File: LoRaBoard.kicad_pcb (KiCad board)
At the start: 2 copper layers, 40.8 x 42 mm, 22 parts, among them J1 CONN_01X12, J2 CONN_01X08, J3 CONN_01X09, J4 CONN_COAXIAL, J5 SwitchSPST, J6 CONN_01X01, J7 PWR, U1 im880b, U2 LDO-TPS78233

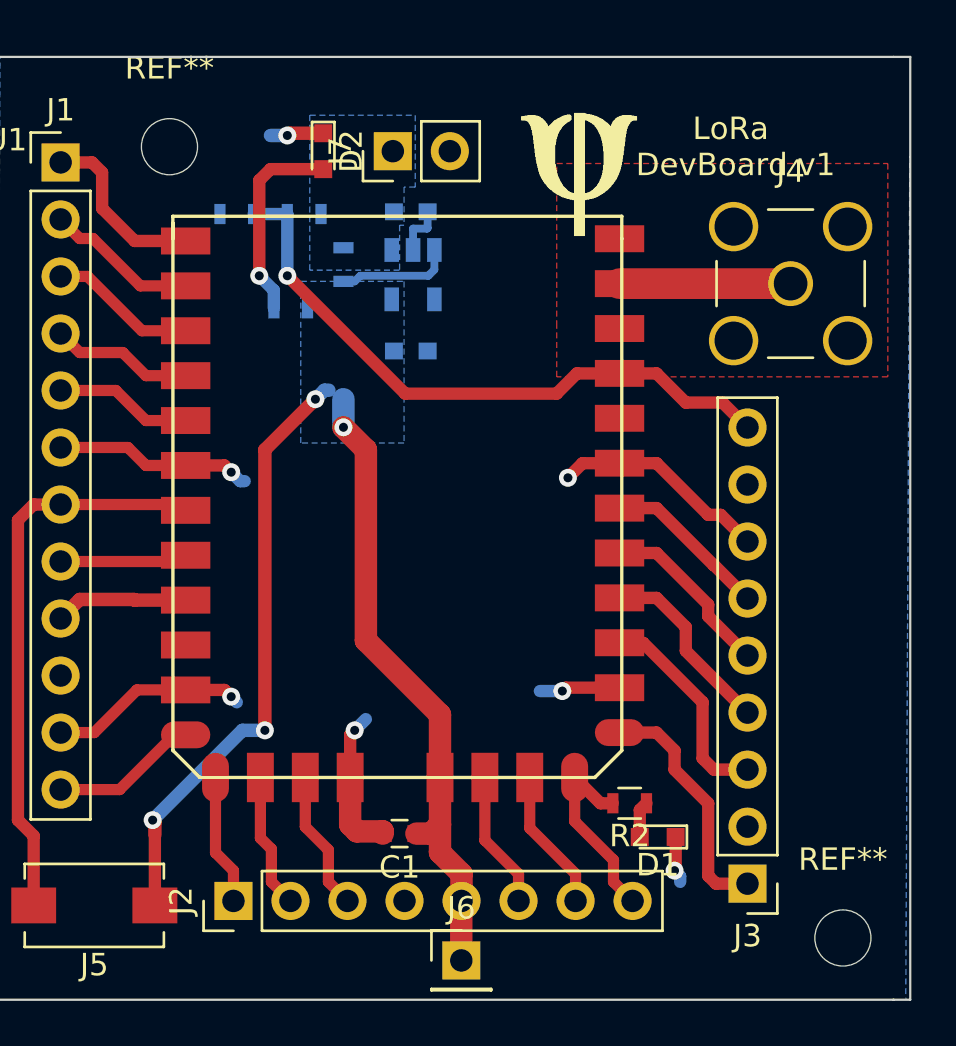
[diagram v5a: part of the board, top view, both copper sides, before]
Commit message: Panelization done, send for Fab
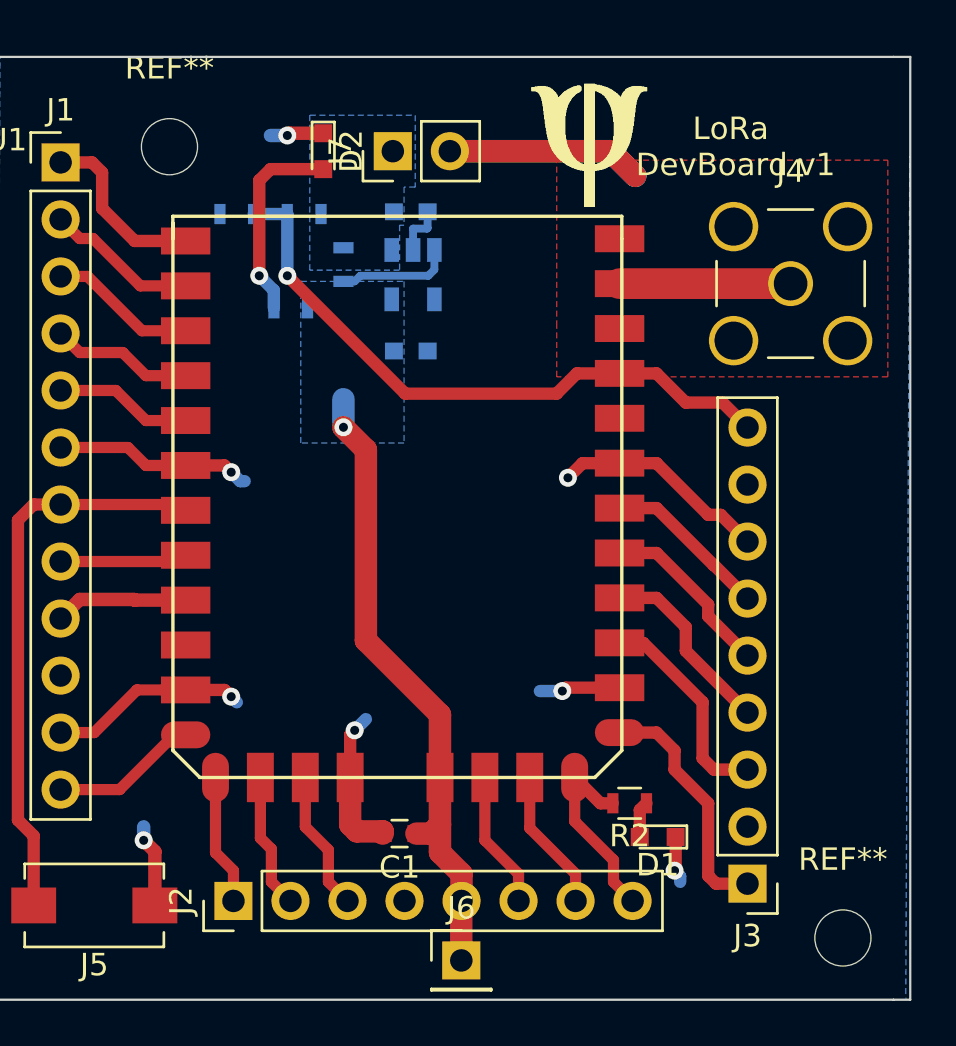
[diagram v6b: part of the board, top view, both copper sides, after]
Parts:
- moved LOGO 1.38 mm to (143.7, 79.2)
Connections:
- J5 pad 1: +3V3 -> GND
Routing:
- net +3V3: track 55.3 -> 28.4 mm, vias 4 -> 1
- net GND: track 44.5 -> 67.6 mm, vias 7 -> 8
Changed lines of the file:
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@@
-(kicad_pcb (version 20170123) (host pcbnew "(2017-04-02 revision 2c33fad45)-master")
+(kicad_pcb (version 4) (host pcbnew 4.0.6-e0-6349~53~ubuntu14.04.1)
   (general
     (links 64)
-    (no_connects 0)
-    (area 117.791667 77.5425 165.953572 121.8425)
+    (no_connects 1)
+    (area 119.949999 77.949999 160.800001 120.050001)
     (thickness 1.6)
     (drawings 12)
-    (tracks 183)
+    (tracks 181)
     (zones 0)
     (modules 22)
@@
   )
   (setup
-    (last_trace_width 1)
+    (last_trace_width 0.6)
     (user_trace_width 0.35)
     (user_trace_width 0.4)
@@
     (trace_clearance 0.2)
     (zone_clearance 0.4)
-    (zone_45_only no)
+    (zone_45_only yes)
     (trace_min 0.2)
     (segment_width 0.2)
@@
       (hpglpenspeed 20)
       (hpglpendiameter 15)
+      (hpglpenoverlay 2)
       (psnegative false)
       (psa4output false)
@@
   )
   (module logo:logo (layer F.Cu)
-    (at 143.25 80.5)
+    (at 143.7 79.2)
     (fp_text reference LOGO (at 0 5) (layer F.SilkS) hide
       (effects (font (thickness 0.3)))
@@
     )
     (pad 1 smd rect (at -2.7 0 180) (size 2 1.6) (layers F.Cu F.Paste F.Mask)
-      (net 2 +3V3))
+      (net 1 GND))
     (pad 2 smd rect (at 2.7 0 180) (size 2 1.6) (layers F.Cu F.Paste F.Mask)
       (net 11 /7))
@@
     )
   )
+  (gr_line (start 160 78) (end 120 78) (layer Edge.Cuts) (width 0.1))
   (gr_line (start 160 78) (end 160.75 78) (layer Edge.Cuts) (width 0.1))
   (gr_line (start 160.75 78) (end 160.75 78) (layer Edge.Cuts) (width 0.1))
@@
   (gr_line (start 120 80) (end 120 80) (layer Edge.Cuts) (width 0.1))
   (gr_line (start 120 78) (end 120 80) (layer Edge.Cuts) (width 0.1))
-  (gr_line (start 160 78) (end 120 78) (layer Edge.Cuts) (width 0.1))
   (gr_text "LoRa\n DevBoard v1\n" (at 152.75 82) (layer F.SilkS)
     (effects (font (size 1 1) (thickness 0.25)))
@@
   (gr_line (start 160 120) (end 120 120) (layer Edge.Cuts) (width 0.1))
   (gr_line (start 120 120) (end 120 80) (layer Edge.Cuts) (width 0.1))
+  (segment (start 126.6 112.9) (end 126.6 112.3) (width 0.6) (layer B.Cu) (net 1))
+  (segment (start 127.1 115.8) (end 127.1 113.4) (width 0.6) (layer F.Cu) (net 1))
+  (segment (start 127.1 113.4) (end 126.6 112.9) (width 0.6) (layer F.Cu) (net 1))
+  (via (at 126.6 112.9) (size 0.8) (drill 0.4) (layers F.Cu B.Cu) (net 1))
+  (segment (start 140.24 82.2) (end 147.4 82.2) (width 1) (layer F.Cu) (net 1))
+  (segment (start 147.4 82.2) (end 148.5 83.3) (width 1) (layer F.Cu) (net 1))
+  (segment (start 140.24 82.2) (end 147.4 82.2) (width 1) (layer B.Cu) (net 1))
+  (segment (start 147.4 82.2) (end 148.5 83.3) (width 1) (layer B.Cu) (net 1))
+  (segment (start 147.4 82.2) (end 148.5 83.3) (width 1) (layer B.Cu) (net 1))
+  (segment (start 140.24 82.2) (end 140.6 82.2) (width 1) (layer B.Cu) (net 1))
   (segment (start 150.5 114.5) (end 150.5 114.75) (width 0.55) (layer B.Cu) (net 1))
   (segment (start 150.25 114.25) (end 150.5 114.5) (width 0.55) (layer B.Cu) (net 1))
@@
   (segment (start 140.75 118.25) (end 140.75 115.61) (width 1) (layer F.Cu) (net 2) (status 30))
   (segment (start 140.75 115.61) (end 140.76 115.6) (width 1) (layer F.Cu) (net 2) (status 30))
-  (segment (start 134.25 93.25) (end 134.649999 92.850001) (width 0.6) (layer B.Cu) (net 2))
-  (segment (start 134.649999 92.850001) (end 134.850001 92.850001) (width 0.6) (layer B.Cu) (net 2))
-  (segment (start 132 108) (end 132 95.5) (width 0.6) (layer F.Cu) (net 2))
-  (segment (start 132 95.5) (end 134.25 93.25) (width 0.6) (layer F.Cu) (net 2))
-  (via (at 134.25 93.25) (size 0.8) (drill 0.4) (layers F.Cu B.Cu) (net 2))
-  (segment (start 127 112) (end 131 108) (width 0.6) (layer B.Cu) (net 2))
-  (segment (start 131 108) (end 132 108) (width 0.6) (layer B.Cu) (net 2))
-  (via (at 132 108) (size 0.8) (drill 0.4) (layers F.Cu B.Cu) (net 2))
-  (segment (start 127.1 112.65) (end 127.1 112.1) (width 0.6) (layer F.Cu) (net 2))
-  (segment (start 127.1 112.1) (end 127 112) (width 0.6) (layer F.Cu) (net 2))
-  (via (at 127 112) (size 0.8) (drill 0.4) (layers F.Cu B.Cu) (net 2))
-  (segment (start 127.1 115.8) (end 127.1 112.65) (width 0.55) (layer F.Cu) (net 2) (status 10))
   (segment (start 135.5 93.25) (end 135.5 94.5) (width 1) (layer B.Cu) (net 2))
   (segment (start 136.5 104) (end 136.5 95.5) (width 1) (layer F.Cu) (net 2))
@@
   )
   (zone (net 1) (net_name GND) (layer F.Cu) (hatch edge 0.508)
-    (priority 1)
+    (priority 4)
     (connect_pads yes (clearance 0.4))
     (min_thickness 0.254)
@@
     (polygon
       (pts
-        (xy 145 90) (xy 145 82.75) (xy 159.75 82.75) (xy 159.75 92.25) (xy 145 92.25)
+        (xy 145 90) (xy 145 82.6) (xy 159.75 82.6) (xy 159.75 92.25) (xy 145 92.25)
       )
     )
@@
       )
     )
+  )
+  (zone (net 0) (net_name "") (layer B.Cu) (hatch edge 0.508)
+    (connect_pads (clearance 0.4))
+    (min_thickness 0.254)
+    (keepout (tracks allowed) (vias allowed) (copperpour not_allowed))
+    (fill yes (arc_segments 16) (thermal_gap 0.508) (thermal_bridge_width 0.508))
+    (polygon
+      (pts
+        (xy 145 81) (xy 163 81) (xy 163 82) (xy 145 82) (xy 145 93)
+        (xy 161 93) (xy 161 94) (xy 144 94) (xy 144 77) (xy 145 77)
+      )
+    )
